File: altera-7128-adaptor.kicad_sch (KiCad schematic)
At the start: 5 parts, among them J1 Conn_01x40_Male, J2 AVR-JTAG-10, J3 Conn_01x40_Male, U1 EPM7128SQC100-7

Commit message: Add initial design
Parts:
- added R1, R2, R3, R4: 1K, Resistor_SMD:R_0805_2012Metric_Pad1.20x1.40mm_HandSolder, symbol Device:R
- C1: footprint Capacitor_SMD:C_0805_2012Metric -> Capacitor_SMD:C_0805_2012Metric_Pad1.18x1.45mm_HandSolder
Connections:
- net +5V: now also R2.1, R3.1, R4.1
- net GND: now also R1.2
- net TCK: now also R1.1
- net TDI: now also R4.2
- net TDO: now also R2.2
- net TMS: now also R3.2
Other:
- moved on the sheet: C1

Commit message: Initial commit
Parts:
- added C2, C3, C4, C5: 100nF, Capacitor_SMD:C_0805_2012Metric_Pad1.18x1.45mm_HandSolder, symbol Device:C
- added J4, J5: Conn_01x03_Male, Connector_PinHeader_2.54mm:PinHeader_1x03_P2.54mm_Vertical, symbol Connector:Conn_01x03_Male
- C1: value C -> 100nF
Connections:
- net +5V: now also C2.1, C3.1, C4.1, C5.1, J5.1 (Pin_1), J5.2 (Pin_2), J5.3 (Pin_3); no longer J2.7 (VCC), J3.1 (Pin_1)
- net GCLK1: now also J3.1 (Pin_1); no longer J1.38 (Pin_38)
- net GND: now also C2.2, C3.2, C4.2, C5.2, J4.1 (Pin_1), J4.2 (Pin_2), J4.3 (Pin_3); no longer J1.40 (Pin_40)
- net OE1: now reaches U1.90 (INPUT/OE1)
- net OE1: now also J1.38 (Pin_38)
- net GCLRN: now reaches U1.91 (INPUT/GCLRN)
- net GCLRN: now also J1.39 (Pin_39)
- net GCLK2 renamed OE2/GCLK2
- net OE2/GCLK2: now also J1.40 (Pin_40); no longer J1.39 (Pin_39)
- no-connect marks 0 -> 3
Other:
- moved on the sheet: C1, J2, R1, R2, R3, R4

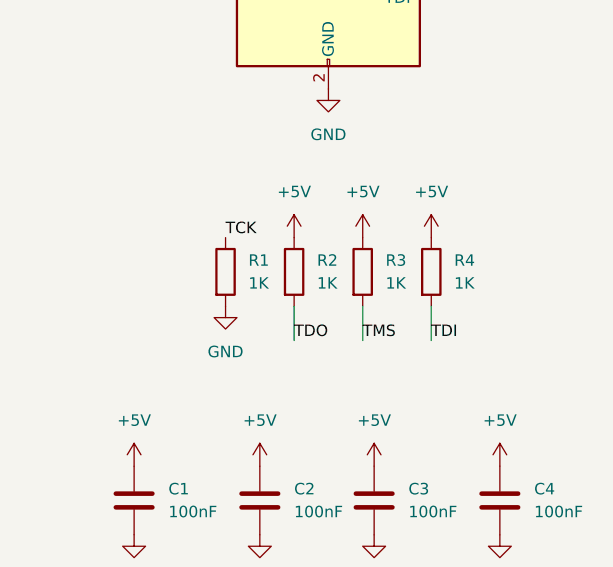
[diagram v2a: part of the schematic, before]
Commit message: Add JTAG resistor values to silkscreen
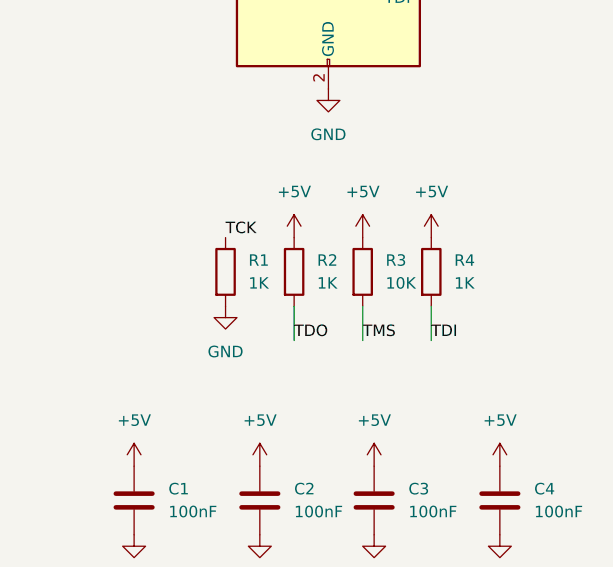
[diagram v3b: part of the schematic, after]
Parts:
- R3: value 1K -> 10K
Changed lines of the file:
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@@
       (effects (font (size 1.27 1.27)) (justify left))
     )
-    (property "Value" "1K" (id 1) (at 251.46 100.3299 0)
+    (property "Value" "10K" (id 1) (at 251.46 100.3299 0)
       (effects (font (size 1.27 1.27)) (justify left))
     )
@@
     )
     (path "/31a6abab-2a1c-4858-a076-141d460f469b"
-      (reference "R3") (unit 1) (value "1K") (footprint "Resistor_SMD:R_0805_2012Metric_Pad1.20x1.40mm_HandSolder")
+      (reference "R3") (unit 1) (value "10K") (footprint "Resistor_SMD:R_0805_2012Metric_Pad1.20x1.40mm_HandSolder")
     )
     (path "/98eb3f75-4d9b-4ccf-90b3-5666550fb465"
